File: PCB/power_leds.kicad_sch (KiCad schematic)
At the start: 26 parts, among them Q301 2N7002, Q302 2N7002, Q303 2N7002, Q304 2N7002

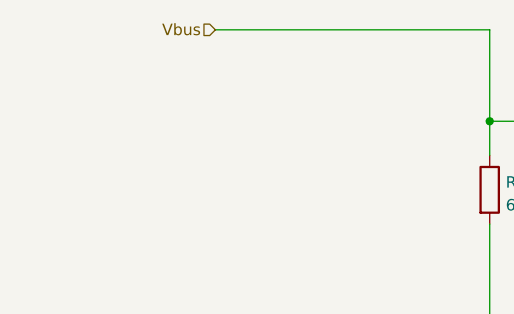
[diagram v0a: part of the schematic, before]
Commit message: Add LEDs for each USBPD level and a microphone
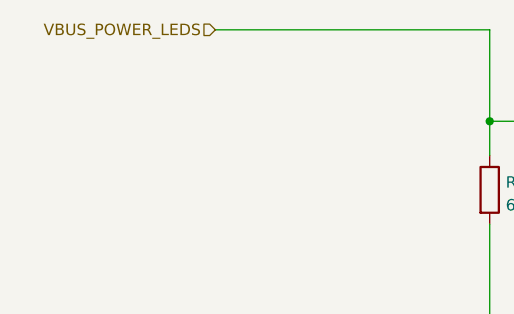
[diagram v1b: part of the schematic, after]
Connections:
- net Vbus renamed VBUS_POWER_LEDS
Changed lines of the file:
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@@
     (effects (font (size 1.27 1.27)) (justify left bottom))
   )
-  (hierarchical_label "Vbus" (shape input) (at 36.83 41.91 180)
+  (hierarchical_label "VBUS_POWER_LEDS" (shape input) (at 36.83 41.91 180)
     (effects (font (size 1.27 1.27)) (justify right))
   )

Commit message: Fix review comments
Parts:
- D304, D305, D306, D307, D308, D309: footprint Skrooter_footprints:LED_0603_1608Metric_smaller_silk -> SkrooterFootprints:LED_0603_1608Metric_smaller_silk
